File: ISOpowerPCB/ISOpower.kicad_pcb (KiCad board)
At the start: 4 copper layers, 199.9 x 99.1 mm, 192 parts, among them J1 XT60_connector_DC_60A_male, J10 USB_CH_A, J11 USB_CH_A, J12 USB_CH_A, J13 USB_CH_A, J14 XT30_connector_DC_30A_female, J15 XT30_connector_DC_30A_female, J16 XT30_connector_DC_30A_female, J17 XT30_connector_DC_30A_female, J18 XT30_connector_DC_30A_female, J19 ESP32_header, J2 ESP_GPIO_B, J20 USB_B_Mini, J21 24vTerminal, J22 12vTerminal, J23 5vTerminal, J24 dio_spare, J25 adc_spare, J26 USB_5v, J29 wifi_header, J3 ESPpin4-7, J30 3V3_spare, J31 USB_B_Mini, J4 SDI-SDO, J5 ESP_GPIO_A, J6 prog_power_select, J7 i2c Header, J8 AVR-ISP-6, J9 USB_CH_A, M1 Fan_IEC60617, Q1 IRF5305_PBF, Q10 BC817, Q11 BC817, Q12 BC817, Q13 BC817, Q14 BC817, Q15 BC817, Q16 BC817, Q17 BC817, Q18 BC817, Q19 BC817, Q2 Si2319CDS, Q20 BC817, Q3 Si2319CDS, Q4 IRF5305_PBF, Q5 IRF5305_PBF, Q6 IRF5305_PBF, Q7 IRF5305_PBF, Q8 IRF5305_PBF, Q9 BC817, SW1 SW_Push, SW2 BOOT, SW3 EN, U1 ESP32-WROOM-32, U10 LM2596S-5, U13 TXS0102DCT, U14 CH340C, U15 TL431DBZ, U16 TL431DBZ, U17 TL431DBZ, U18 TL431DBZ, U19 HEF4093B, U2 AMS1117-3.3, U3 ATmega328PB-M, U4 i6A4W020A-DC-DC-250W, U5 i6A4W020A-DC-DC-250W, U6 ACS712xLCTR-30A, U7 ACS712xLCTR-30A, U8 CH340C, Y1 16MHz

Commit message: sdfs
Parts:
- J8: value AVR-ISP-6 -> AVR-ISP
- R6: value 5V_BUS_TRIM -> 5v_trim
- R7: value BUS_A_trim -> 12v_trim
- moved R4b1 0.64 mm to (97.8, 125.1), turned to -90 degrees
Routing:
- net 12V_BUS: track 208.1 -> 222.4 mm
- net Net-(R3b1-Pad2): track 15.6 -> 12.7 mm
- net 5V_BUS: track 274.5 -> 277.1 mm
- net GNDPWR: track 210.1 -> 208.7 mm, vias 32 -> 31

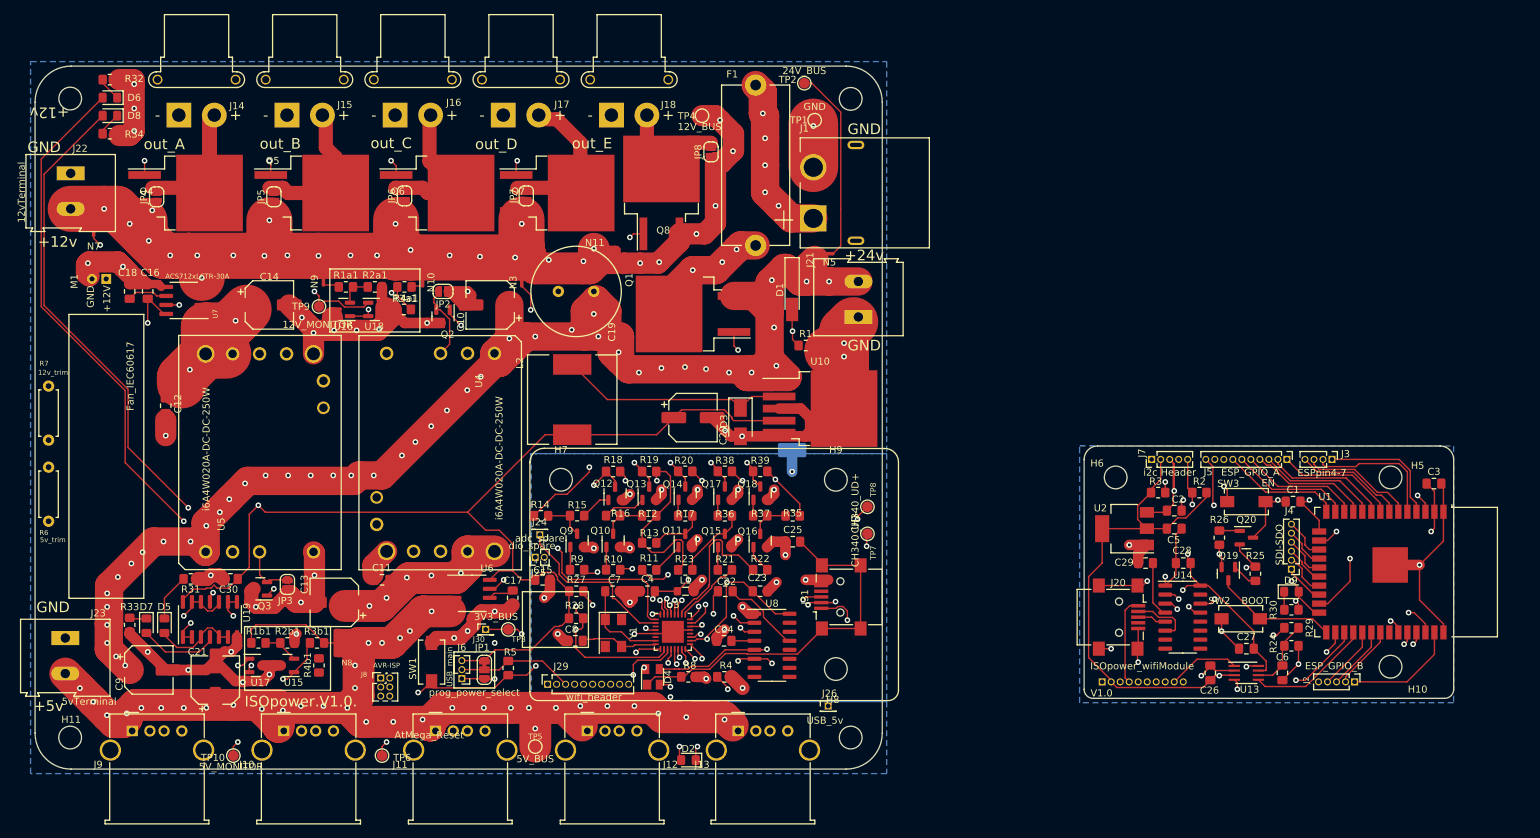
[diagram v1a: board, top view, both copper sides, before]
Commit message: Finished Silkscreen edits
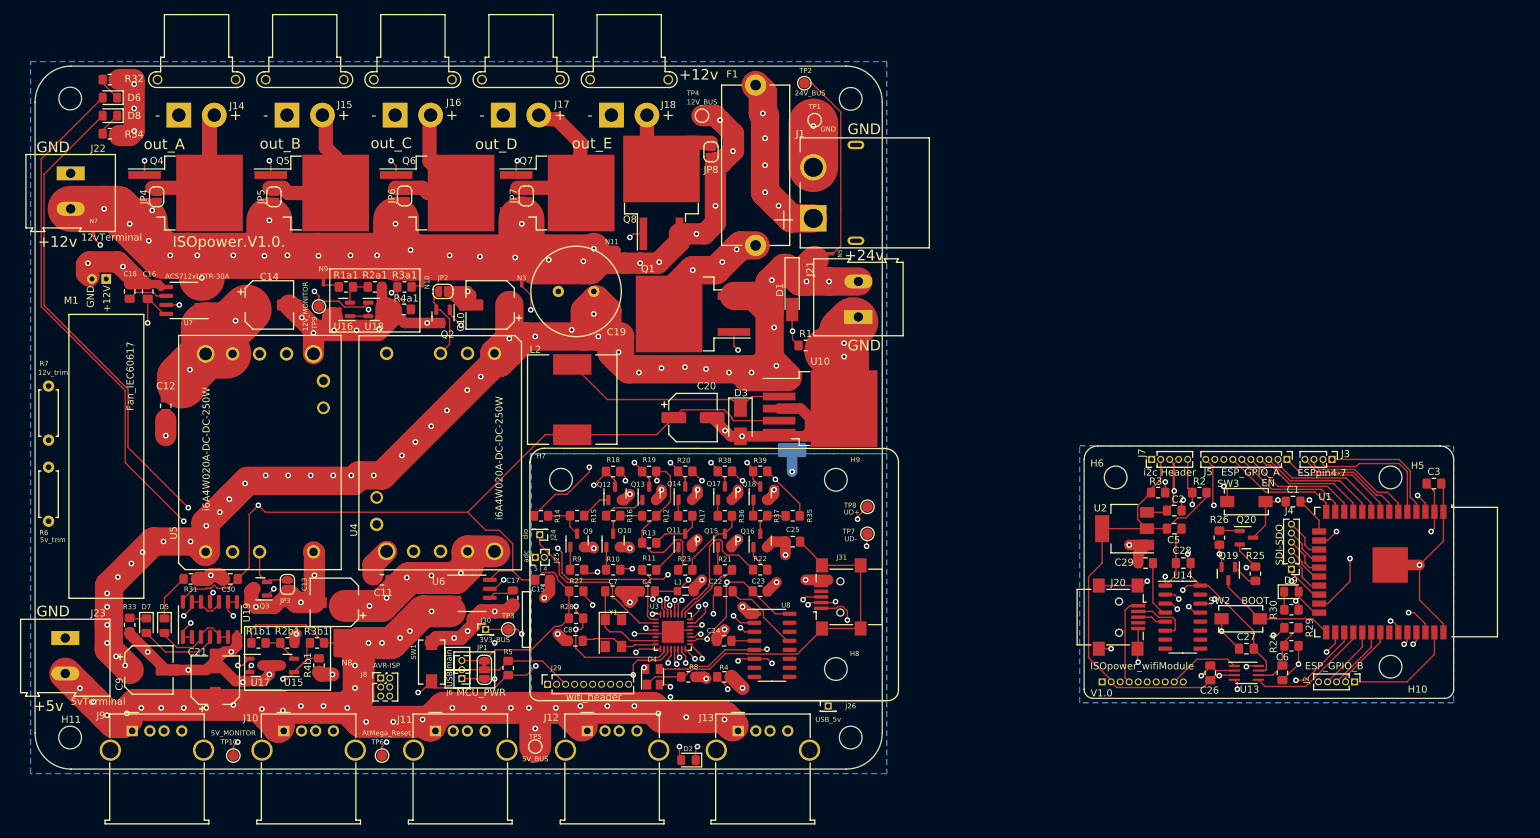
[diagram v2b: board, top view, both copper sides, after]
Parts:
- J24: value dio_spare -> dio
- J25: value adc_spare -> adc
- JP1: value prog_power_select -> MCU_PWR
- TP7: value CH340_UD- -> UD-
- TP8: value CH340_UD+ -> UD+
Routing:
- net 12V_BUS: track 222.4 -> 232.7 mm
- net Net-(R3b1-Pad2): track 12.7 -> 17.1 mm
- net GNDPWR: track 208.7 -> 210.7 mm, vias 31 -> 32
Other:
- board text added: "5 | 4"
- board text removed: "4 | 5"

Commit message: Passed DRC - Board separation into 2 folders next
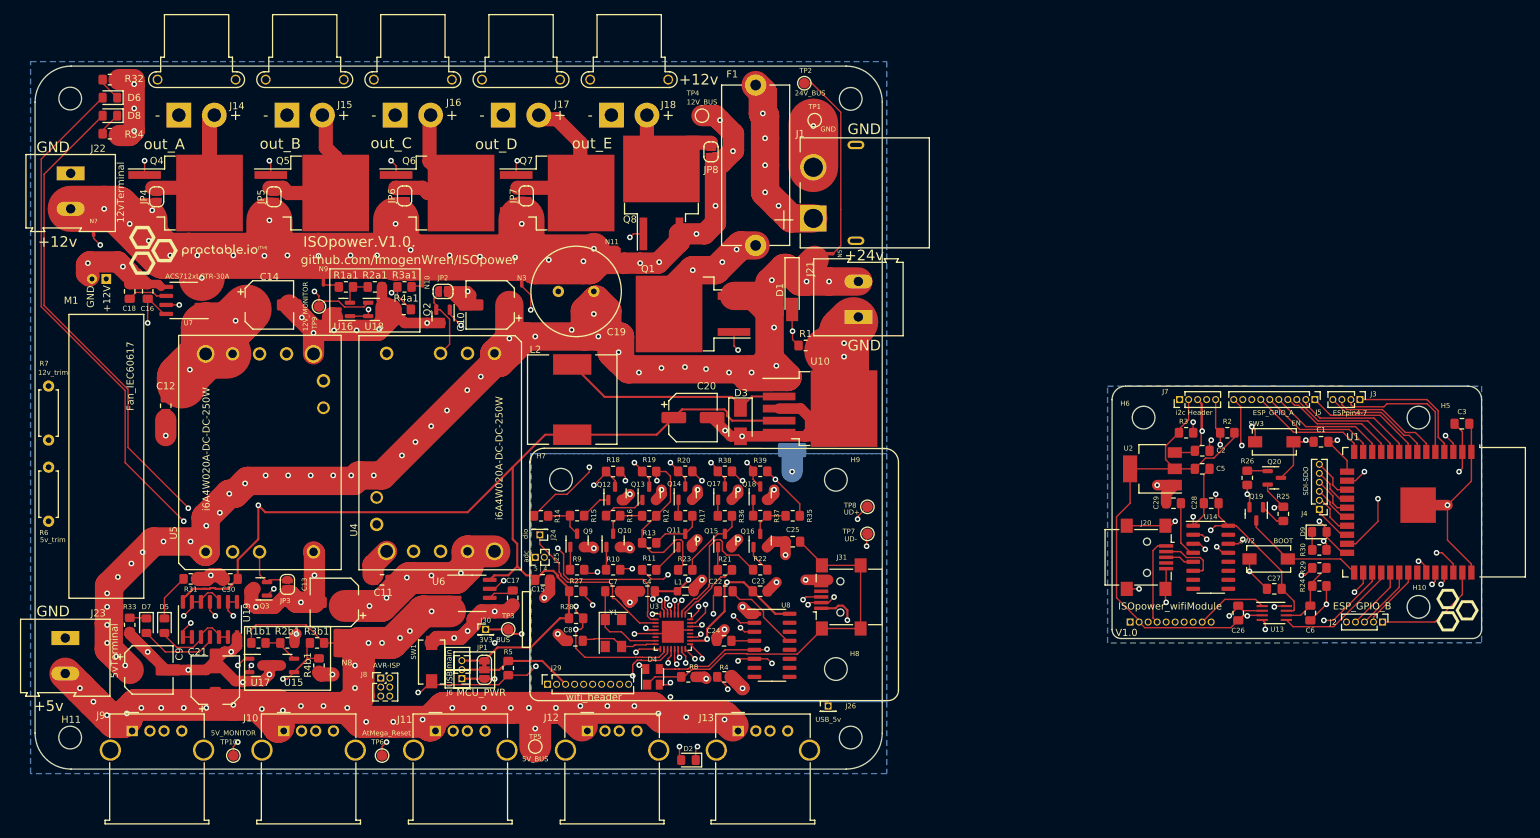
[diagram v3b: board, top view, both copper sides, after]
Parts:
- added G***: LOGO, 000_Graphics_Immo:practactable.io_symbol_7x6, F.Cu at (257.9, 117.3)
- added G***: LOGO, 000_Graphics_Immo:practactable.io_text_20x8, F.Cu at (80.6, 66.7)
- added G***: LOGO, 000_Graphics_Immo:practactable.io_text_50x20, B.Cu at (236.3, 106.5)
- added G***: LOGO, 000_Graphics_Immo:practactable.io_text_30x11_SM, B.Cu at (136.5, 89.5)
- moved C1 9.31 mm to (239.0, 93.6)
- moved C2 9.31 mm to (222.2, 94.8)
- moved C26 9.31 mm to (227.3, 117.7)
- moved C28 9.31 mm to (223.5, 102.2)
- moved C29 9.31 mm to (218.2, 102.2)
- moved C3 9.31 mm to (258.8, 91.0)
- moved C6 9.31 mm to (237.5, 117.7)
- moved H6 9.31 mm to (214.0, 90.2)
- moved J5 9.31 mm to (238.1, 87.6)
- moved J7 9.31 mm to (219.1, 87.6)
- moved Q19 9.31 mm to (229.9, 103.7)
- moved R25 9.31 mm to (233.7, 103.7)
- moved U1 9.31 mm to (251.9, 103.5)
- moved C27 9.31 mm to (232.4, 114.3)
- moved C5 9.31 mm to (222.2, 97.4)
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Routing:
- net MCU_5V: track 187.4 -> 198.5 mm
- net Net-(D8-Pad2): track 81.1 -> 86.2 mm
- net Net-(R6-Pad1): track 61.7 -> 59.1 mm
- net /USB_PBUS: track 74.6 -> 77.1 mm
- net /AtMega328p/MCU_5V_BUS: track 95.0 -> 96.0 mm
- net Net-(D6-Pad2): track 91.1 -> 91.8 mm
- net Net-(D5-Pad2): track 10.9 -> 11.6 mm
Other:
- board size 199.9 x 99.1 mm -> 203.8 x 99.1 mm
- board text added: "github.com/ImogenWren/ISOpower"
